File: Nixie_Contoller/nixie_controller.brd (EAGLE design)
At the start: 111.7 x 49.2 mm, 28 parts, among them IC1 DS1307, IC2 7805TV, J1 CON-SOCJ-2155, SW1 EC12E_SW, U1 328P, U2 HU2032-LF, Y2 32.768kHz

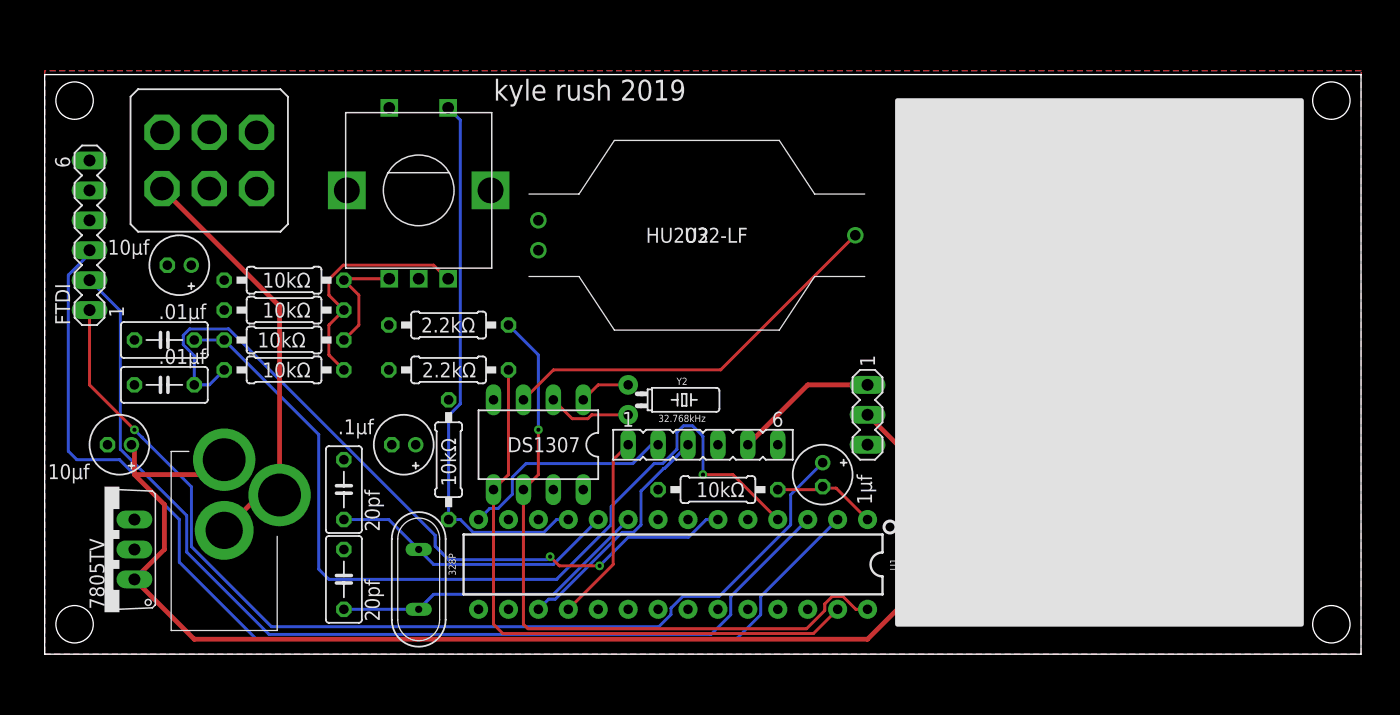
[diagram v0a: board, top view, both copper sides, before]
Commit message: Changes to vertical mounted encoder and switch on base
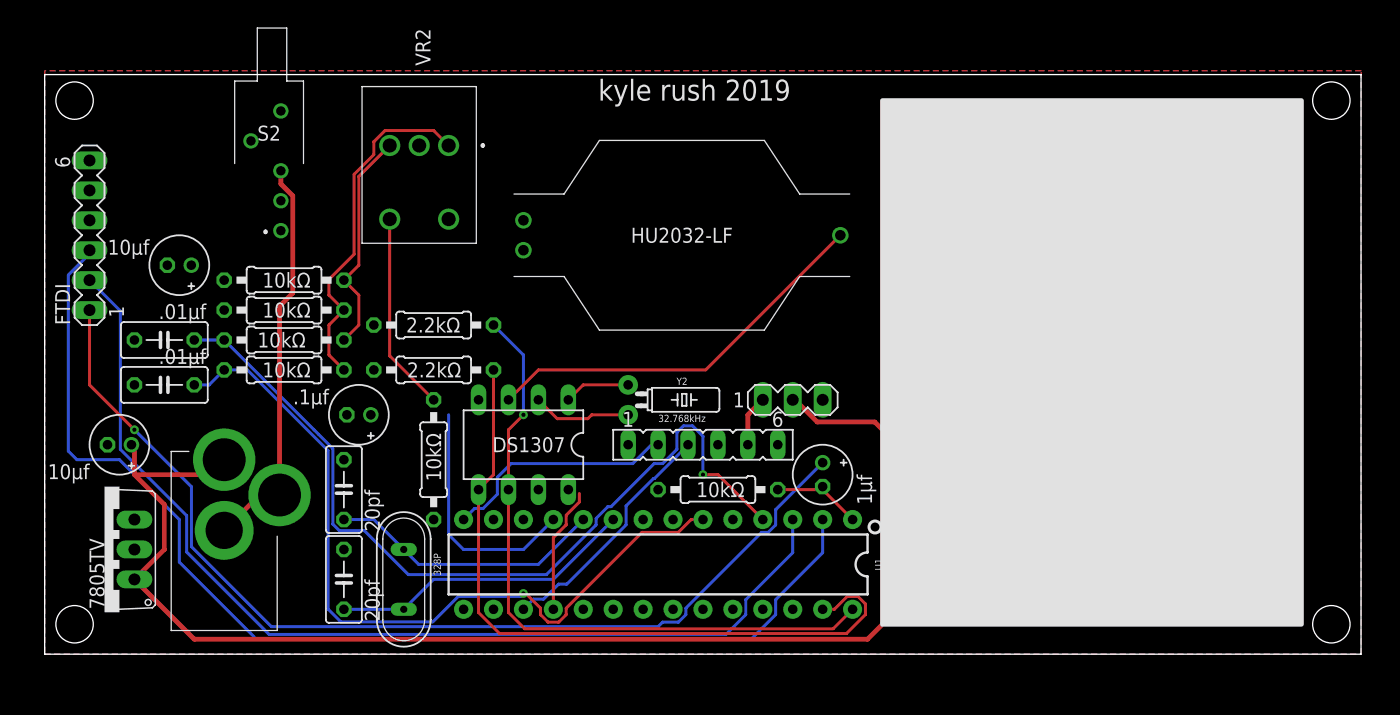
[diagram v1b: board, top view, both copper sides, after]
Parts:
- removed S1: (no value), switch:320-938
- removed SW1: EC12E_SW, switch-alps:ALPS_EC12E_SW
- added S2: A12AV, SamacSys_Parts:A12AV
- added VR2: PEC09-2220F-S0012, SamacSys_Parts:PEC092220FS0012
- Q1: value (none) -> 16MHz
- moved SV2 6.48 mm to (63.5, 21.6), turned to 0 degrees
- moved C5 4.58 mm to (26.7, 20.3)
- moved U1 1.27 mm to (52.1, 7.62)
- moved Q1 1.27 mm to (30.5, 6.35)
- moved IC1 1.27 mm to (40.6, 17.8)
- moved R1 1.27 mm to (33.0, 27.9)
- moved R2 1.27 mm to (33.0, 24.1)
- moved R7 1.27 mm to (33.0, 16.5), turned to 270 degrees
- moved U2 1.27 mm to (40.6, 36.8)
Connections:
- net GND: now also S2.2, S2.4, S2.5, VR2.C1, VR2.D1; no longer S1.2, S1.3, SW1.C, SW1.D, SW1.GND1, SW1.GND2
- net N$15: now also VR2.B1; no longer SW1.A
- net N$2: now also VR2.E1; no longer SW1.E
- net N$3: now also VR2.A1; no longer SW1.B
- net N$6: now also S2.3; no longer S1.1
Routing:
- net N$3: track 20.4 -> 29.8 mm
- net N$2: track 46.8 -> 37.5 mm
- net N$15: track 10.0 -> 19.3 mm
- net N$13: track 52.5 -> 60.6 mm
- net V+: track 12.3 -> 4.34 mm
- net +12V: track 107.3 -> 114.1 mm
- net CLK: track 16.1 -> 10.7 mm
- net N$9: track 77.0 -> 71.9 mm
- net N$10: track 64.0 -> 66.7 mm, vias 2 -> 1
- net N$12: track 58.3 -> 56.4 mm
- net N$6: track 36.1 -> 34.3 mm
- net N$5: track 7.15 -> 8.42 mm
- net N$16: track 24.7 -> 23.5 mm
- net N$14: track 8.96 -> 7.69 mm
- net N$11: track 27.3 -> 26.0 mm
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
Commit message: small big fixes
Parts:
- moved C1 2.84 mm to (3.81, 19.1)
- moved IC2 1.80 mm to (6.35, 10.2), turned to 270 degrees
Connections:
- net +12V: now also S2.3; no longer J1.1
- net GND: now also J1.2, J1.3; no longer S2.2
- net N$6: now also J1.1, S2.2; no longer J1.2, J1.3, S2.3
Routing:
- net +12V: track 114.1 -> 137.1 mm
- net N$6: track 34.3 -> 24.8 mm
- net CLK: track 10.7 -> 16.6 mm
- net N$22: track 97.2 -> 95.2 mm
- net N$2: track 37.5 -> 39.3 mm
- net N$18: track 20.0 -> 20.7 mm
- net N$7: track 19.4 -> 20.0 mm

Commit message: Snapshot 12-23
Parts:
- removed SV2: (no value), con-lstb:MA03-1
- added C10: 100uF,35V, nick:C-EIA-7343
- added C11, C9: 100n, rcl:C0805
- added C12: 4u7,250V, nick:NICHICON-UJ-12
- added C13: 100n,250V, nick:C2420
- added C14: 10uF,25V, nick:C-EIA-7343
- added D1: ES2F, diode:SMC
- added IC3: 7805T, linear:TO220H
- added L1: 100uH, nick:L-B82479
- added R10: 10K, rcl:R0805
- added R9: 1M5, rcl:R2512
- added RSENSE: 0R050, rcl:R2010
- added T1: IRF644PBF, transistor-power:TO220BV
- added VR1: 5K, nick:BOURNS-3214W
- IC2: value 7805TV -> MAX1771ESA; device linear:TO220V -> nick:SO-8
- moved IC2 83.9 mm to (88.8, 25.3), turned to 180 degrees
- moved FTDI 24.3 mm to (6.35, 11.4)
- moved C5 22.5 mm to (48.3, 14.0), turned to 0 degrees
- moved C3 20.5 mm to (30.5, 29.2), turned to 0 degrees
- moved C4 20.5 mm to (30.5, 25.4), turned to 0 degrees
- moved R1 13.7 mm to (20.3, 22.9)
- moved R2 13.3 mm to (20.3, 20.3)
- moved C2 11.5 mm to (10.2, 21.6), turned to 270 degrees
- moved J1 3.81 mm to (15.2, 12.7)
- moved C1 3.81 mm to (3.81, 22.9)
- moved S2 2.54 mm to (21.6, 44.5)
- moved C8 1.80 mm to (67.3, 14.0), turned to 90 degrees
- moved R3 1.27 mm to (20.3, 33.0)
- moved R8 1.27 mm to (58.4, 14.0)
- moved U1 1.27 mm to (52.1, 6.35)
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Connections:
- new net EXT: IC2.1, T1.G
- new net N$19: D1.A, L1.P$2, T1.D
- new net N$20: C9.1, IC2.5
- new net N$23: R10.2, VR1.1, VR1.2
- new net N$24: IC2.8, RSENSE.2, T1.S
- new net N$8: IC2.3, R9.1, VR1.3
- net +12V: now also C10.+, C11.1, C14.+, IC2.2, IC3.1, L1.P$1; no longer IC2.1, SV2.2
- net GND: now also C10.-, C11.2, C12.1, C13.P$2, C14.-, C9.2, IC2.4, IC2.6, IC2.7, IC3.2, R10.1, RSENSE.1; no longer IC2.2, SV2.3
- net V+: now also C12.2, C13.P$1, D1.C, R9.2; no longer SV2.1
- net VCC: now also IC3.3; no longer IC2.3
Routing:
- net N$10: track 66.7 -> 39.2 mm, vias 1 -> 0
- net N$22: track 95.2 -> 68.6 mm, vias 0 -> 1
- net N$9: track 71.9 -> 45.8 mm, vias 1 -> 0
- net V+: track 4.34 -> 25.8 mm
- net GND: track 0.00 -> 20.4 mm, vias 0 -> 97
- net N$21: track 87.3 -> 68.6 mm
- net N$8: track 0.00 -> 12.2 mm
- net N$17: track 86.9 -> 75.4 mm, vias 1 -> 0
- net N$13: track 60.6 -> 51.7 mm
- net CLK: track 16.6 -> 25.0 mm
- net N$23: track 0.00 -> 7.35 mm
- net N$18: track 20.7 -> 26.0 mm
- net N$15: track 19.3 -> 24.0 mm
- net N$6: track 24.8 -> 28.8 mm
- net N$20: track 0.00 -> 3.77 mm
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- added copper zone on layer 1, net +12V
- added copper zone on layer 1, net EXT
- added copper zone on layer 16, net GND
- added copper zone on layer 1, net N$19
- added copper zone on layer 1, net N$24
- added copper zone on layer 1, net V+
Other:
- board size 111.7 x 49.2 mm -> 113 x 51.7 mm
- board text added: "0.000"
- board text added: "0.001"
- board text added: "0.146"
- board text added: "0.154"
- board text added: "1.209"
- board text added: "1.508"
- board text added: "1.512"
- board text added: "1.655"
- board text added: "1.839"
- board text added: "2.026"

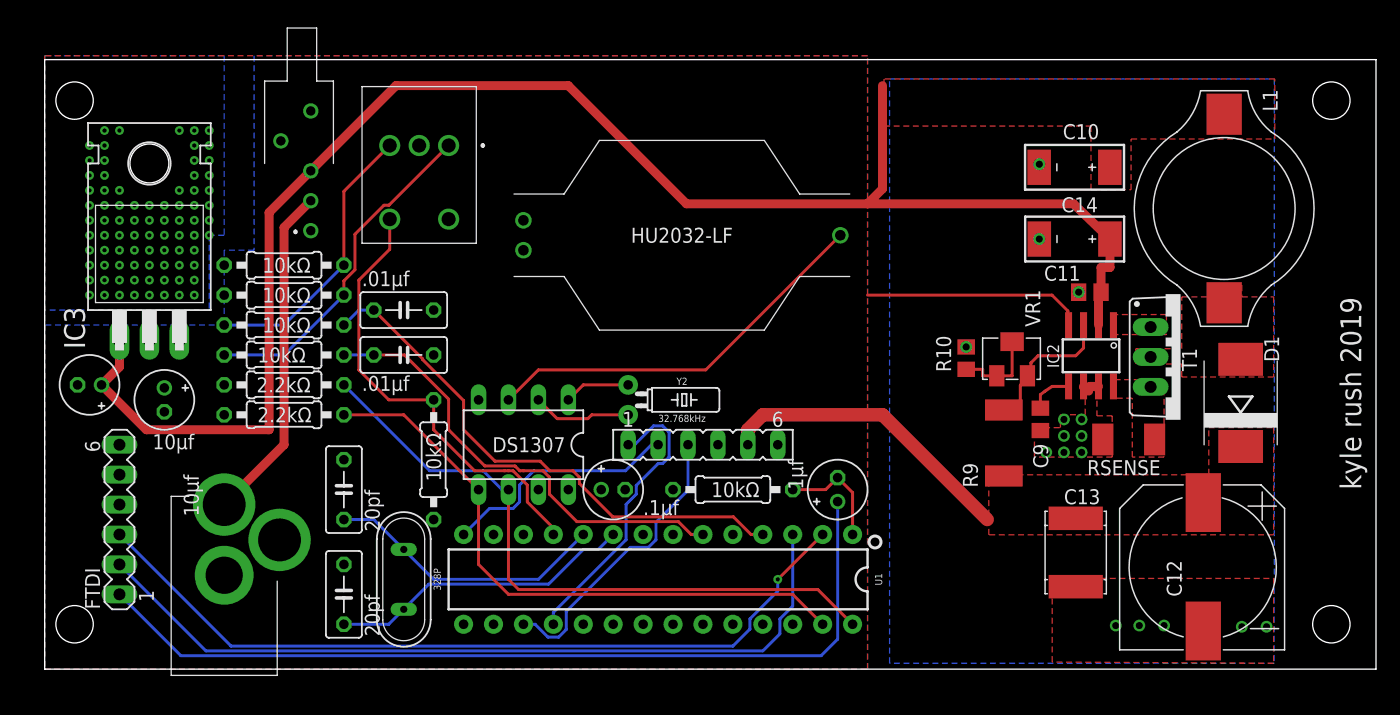
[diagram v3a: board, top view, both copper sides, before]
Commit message: Shrinks board size, uses SMD components
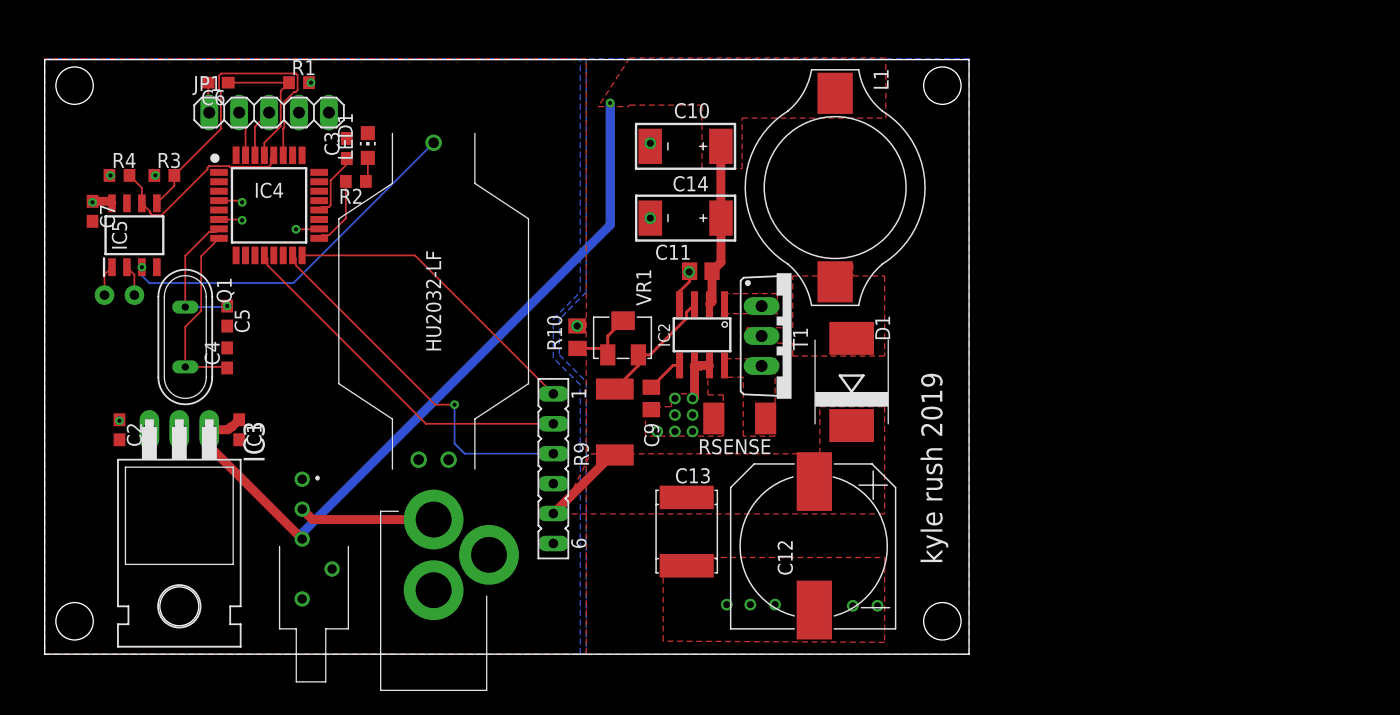
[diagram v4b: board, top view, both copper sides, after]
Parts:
- removed C8: 1μf, rcl:E2-5
- removed FTDI: (no value), con-lstb:MA06-1
- removed IC1: DS1307, adafruit:DIL08
- removed R5, R6, R7, R8: 10kΩ, rcl:0207/10
- removed U1: 328P, SparkFun-IC-Microcontroller:DIP28
- removed VR2: PEC09-2220F-S0012, SamacSys_Parts:PEC092220FS0012
- added IC4: ATMEGA328P-AUR, SamacSys_Parts:QFP80P900X900X120-32N
- added IC5: DS1307Z+T_R, SamacSys_Parts:SOIC127P600X175-8N
- added JP1: FTDI, pinhead:1X05
- added LED1: (no value), led:CHIP-LED0805
- C1, C2: value 10μf -> 10μF; device rcl:E2-5 -> rcl:C0603
- C3: value .01μf -> .1μF; device rcl:C050-030X075 -> rcl:C0603
- C4: value .01μf -> 20PF; device rcl:C050-030X075 -> rcl:C0603
- C5: value .1μf -> 20PF; device rcl:E2-5 -> rcl:C0603
- C6: value 20pf -> 1μF; device rcl:C050-030X075 -> rcl:C0603
- C7: value 20pf -> .1μF; device rcl:C050-030X075 -> rcl:C0603
- R1: value 2.2kΩ -> 10k; device rcl:0207/10 -> rcl:R0603
- R2: value 2.2kΩ -> 330; device rcl:0207/10 -> rcl:R0603
- R3, R4: value 10kΩ -> 2.2k; device rcl:0207/10 -> rcl:R0603
- moved C6 44.7 mm to (14.7, 48.5), turned to 180 degrees
- moved Y2 44.1 mm to (6.35, 30.5), flipped to the bottom, turned to 180 degrees
- moved S2 38.1 mm to (22.9, 6.35), turned to 0 degrees
- moved C5 35.9 mm to (15.5, 28.7), turned to 270 degrees
- moved C14 33.1 mm to (54.4, 37.0)
- moved L1 33.1 mm to (67.1, 39.6)
- moved C10 33.1 mm to (54.4, 43.1)
- moved R9 33.1 mm to (48.4, 19.7)
- moved T1 33.1 mm to (63.4, 27.0)
- moved VR1 33.1 mm to (49.1, 26.8)
- moved C11 33.1 mm to (55.7, 32.5)
- moved C12 33.1 mm to (67.7, 11.3)
- moved C13 33.1 mm to (54.5, 10.4)
- moved C9 33.1 mm to (51.5, 21.7)
- moved D1 33.1 mm to (68.5, 23.1)
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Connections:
- removed net N$15: R3.1, R5.2, VR2.B1
- removed net N$21: FTDI.2, U1.3
- removed net N$22: FTDI.3, U1.2
- new net RST: C6.1, IC4.29, R1.1
- net +12V: now also C1.1; no longer C1.+
- net CLK: now also IC4.16; no longer U1.18
- net GND: now also C1.2, C2.2, C5.2, IC4.21, IC4.3, IC4.5, IC5.4, JP1.5, LED1.C; no longer C1.-, C2.-, C5.-, C6.2, FTDI.6, IC1.4, U1.22, U1.8, VR2.C1, VR2.D1
- net N$1: now also IC5.3; no longer IC1.3
- net N$10: now also LED1.A, R2.1; no longer C4.1, R6.2, U1.6
- net N$11: now also C5.1, IC4.7; no longer C6.1, U1.9
- net N$12: now also IC4.27, IC5.5, R3.2; no longer IC1.6, R1.1, U1.28
- net N$13: now also IC4.28, IC5.6, R4.2; no longer IC1.5, R2.2, U1.27
- net N$14: now also IC4.30, JP1.3; no longer C8.-, R8.1, U1.1
- net N$16: now also C4.1, IC4.8; no longer C7.1, U1.10
- net N$17: now also C6.2, JP1.1; no longer C8.+, FTDI.1
- net N$18: now also IC4.15; no longer U1.17
- net N$2: now also IC4.31, JP1.2; no longer R7.1, U1.11, VR2.E1
- net N$3: now also IC4.17, R2.2; no longer R4.1, R6.1, VR2.A1
- net N$4: now also IC5.2, Y2.2; no longer IC1.1, Y2.1
- net N$5: now also IC5.1, Y2.1; no longer IC1.2, Y2.2
- net N$7: now also IC4.12; no longer U1.14
- net N$9: now also IC4.20; no longer R5.1, U1.4
- net VCC: now also C2.1, C7.1, IC4.18, IC4.4, IC4.6, IC5.8, JP1.4, R3.1, R4.1; no longer C2.+, C5.+, FTDI.4, IC1.8, R2.1, R3.2, R4.2, R7.2, R8.2, U1.20, U1.7
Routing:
- net N$17: track 75.4 -> 2.58 mm
- net N$22: track 68.6 -> 0.00 mm, vias 1 -> 0
- net N$21: track 68.6 -> 0.00 mm
- net +12V: track 140.0 -> 77.1 mm, vias 0 -> 1
- net N$9: track 45.8 -> 5.69 mm
- net N$10: track 39.2 -> 2.07 mm
- net N$2: track 38.8 -> 3.85 mm
- net N$13: track 51.7 -> 17.1 mm
- net N$12: track 56.1 -> 27.3 mm
- net N$15: track 24.0 -> 0.00 mm
- net N$3: track 28.9 -> 6.11 mm
- net V+: track 25.8 -> 7.28 mm
- net N$6: track 28.8 -> 11.5 mm
- net N$11: track 26.0 -> 11.7 mm, vias 0 -> 1
- net GND: track 20.4 -> 6.70 mm, vias 97 -> 16
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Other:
- board size 113 x 51.7 mm -> 78.5 x 50.5 mm

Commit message: Snapshot 12/27
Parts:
- moved C4 1.52 mm to (17.0, 25.1)
- moved C5 1.52 mm to (17.0, 28.7)
- moved Q1 1.52 mm to (13.5, 26.9)
- turned SV1 to 90 degrees
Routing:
- net CLK: track 26.2 -> 41.1 mm
- net N$7: track 30.8 -> 34.1 mm
- net V+: track 7.28 -> 6.32 mm
- net N$18: track 31.4 -> 30.5 mm
- net N$11: track 11.7 -> 11.1 mm
- net N$16: track 15.7 -> 15.1 mm
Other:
- board size 78.5 x 50.5 mm -> 76.2 x 50.7 mm
